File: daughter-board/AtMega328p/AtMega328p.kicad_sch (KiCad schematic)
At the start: 49 parts, among them J1 Conn_02x10_Odd_Even, J2 Conn_02x10_Odd_Even, U1 STM32L462CETx, Y1 Crystal_Small

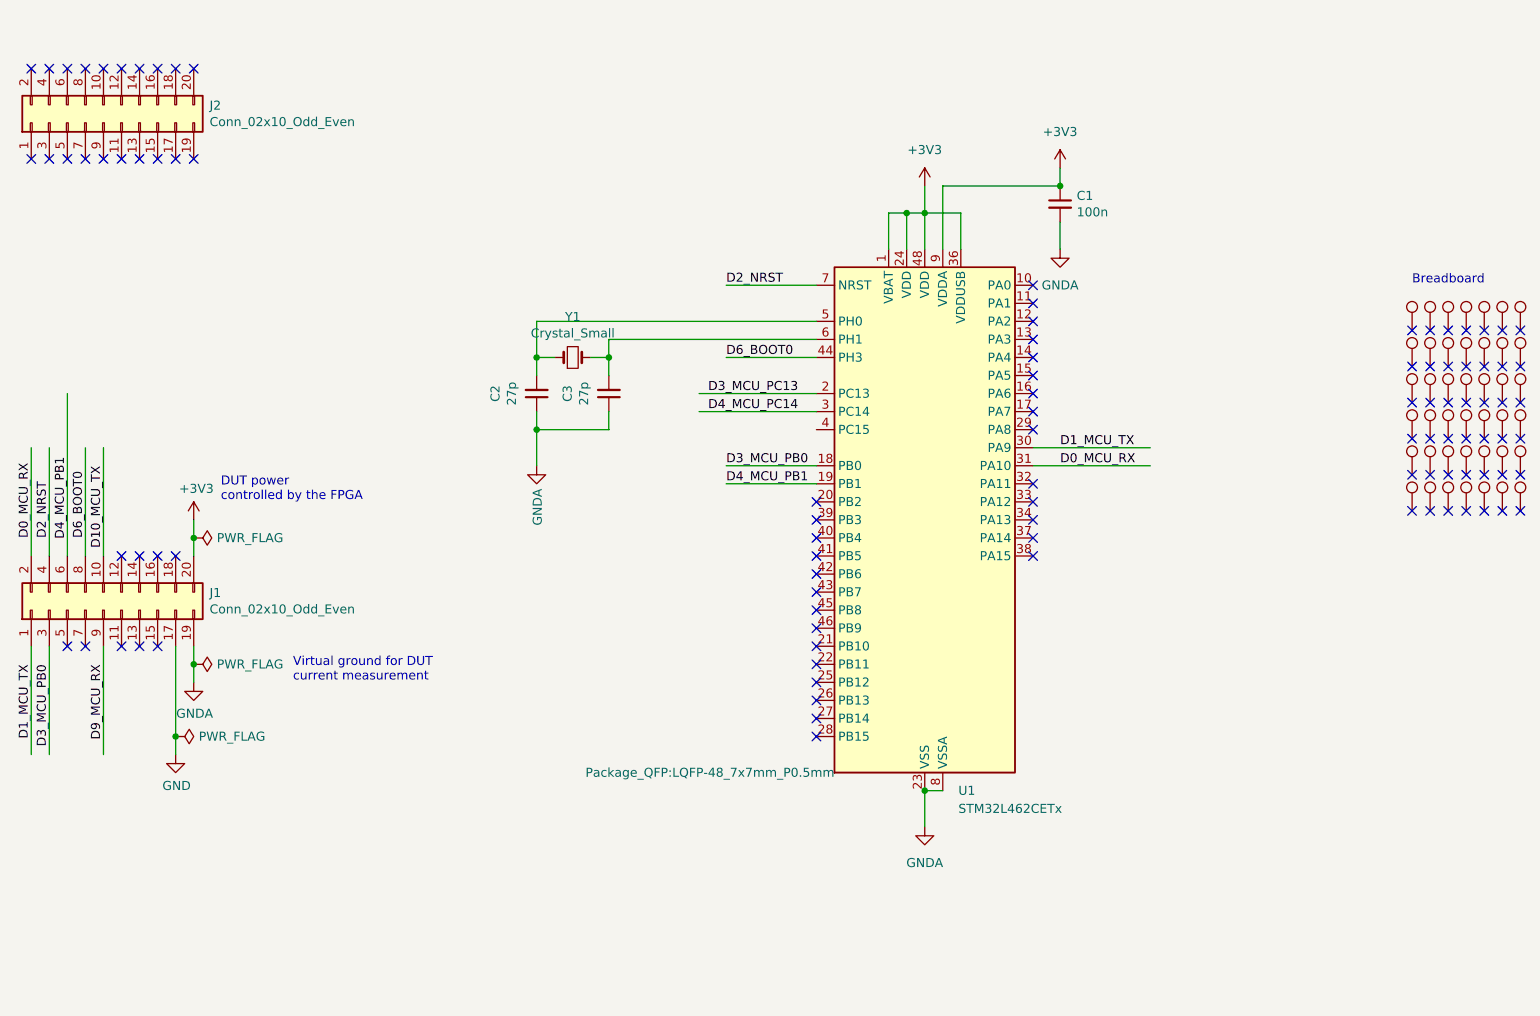
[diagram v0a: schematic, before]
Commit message: l462 routing -  Add ATMega board - Update ceval script
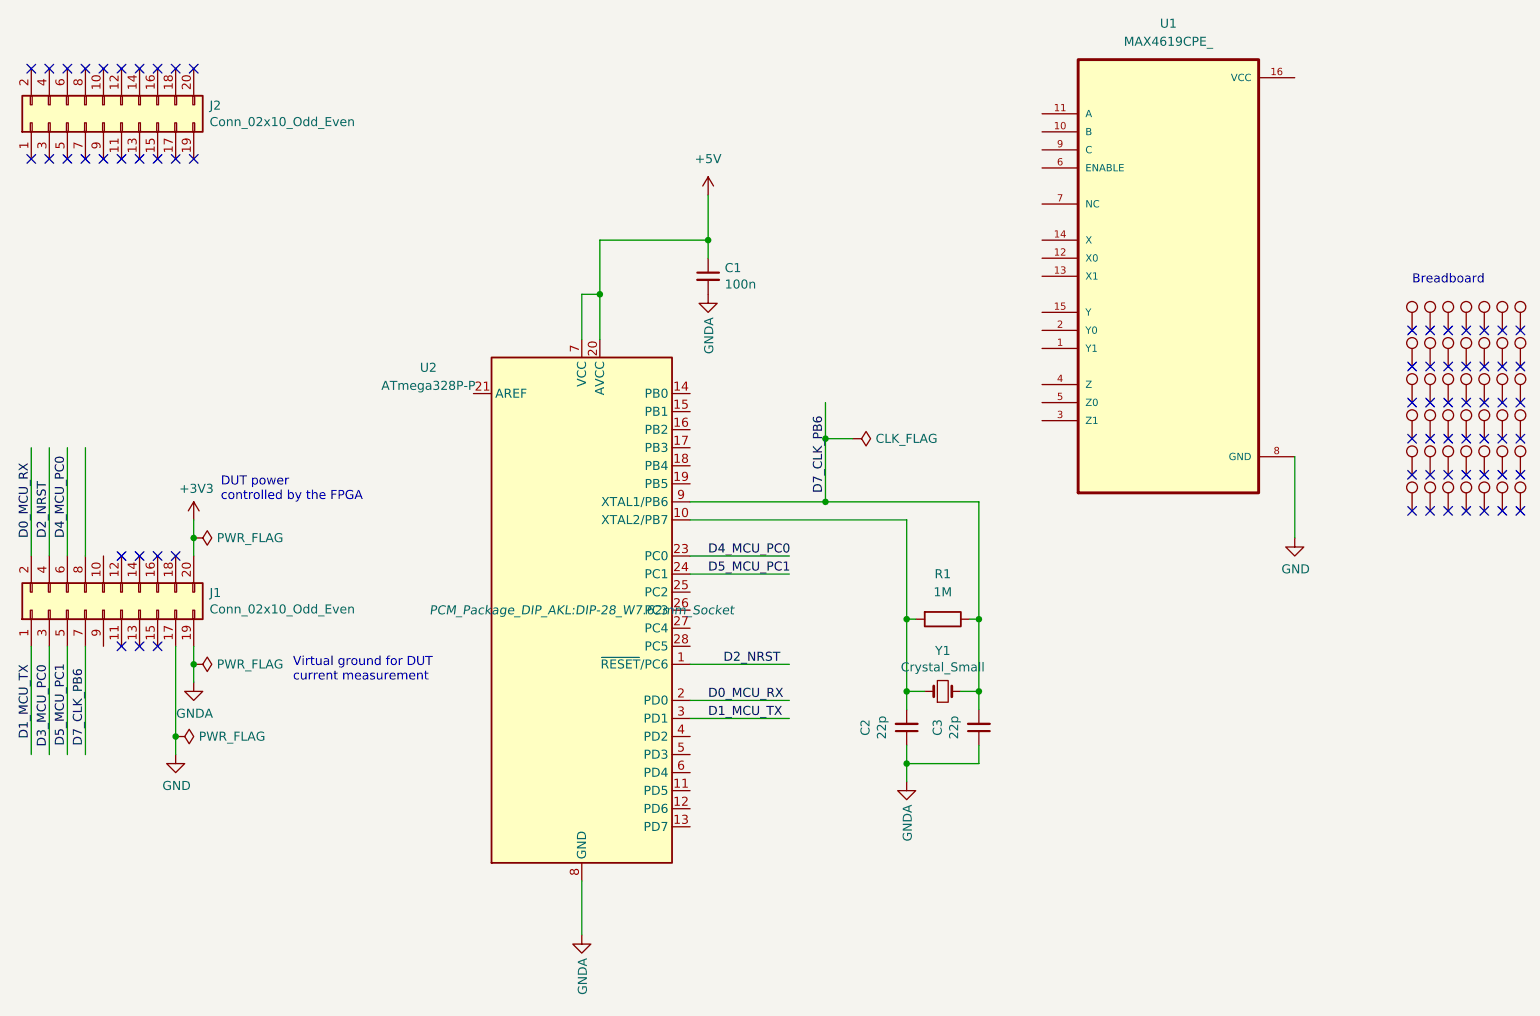
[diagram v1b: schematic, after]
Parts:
- removed U1: STM32L462CETx, Package_QFP:LQFP-48_7x7mm_P0.5mm, symbol PCM_MCU_ST_STM32L4:STM32L462CETx
- added R1: 1M, PCM_Resistor_SMD_AKL:R_0402_1005Metric, symbol Device:R
- added U1: MAX4619CPE_, MAX4619CPE_:DIP794W47P254L1943H457Q16, symbol MAX4619CPE_:MAX4619CPE_
- added U2: ATmega328P-P, PCM_Package_DIP_AKL:DIP-28_W7.62mm_Socket, symbol MCU_Microchip_ATmega:ATmega328P-P
- C1: footprint PCM_Capacitor_SMD_AKL:C_0805_2012Metric -> PCM_Capacitor_SMD_AKL:C_0201_0603Metric
- C2, C3: value 27p -> 22p
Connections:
- net +3V3: no longer C1.1
- net D0_MCU_RX: now also U2.2 (PD0)
- net D1_MCU_TX: now also U2.3 (PD1)
- net D2_NRST: now also U2.1 (~{RESET}/PC6)
- net GND: now also U1.8 (GND)
- net GNDA: now also U2.22 (GND), U2.8 (GND)
- net at C2.2, Y1.1: now also R1.2, U2.10 (XTAL2/PB7)
- net D7_CLK_PB6: now reaches C3.2, Y1.2
- net D7_CLK_PB6: now also J1.7 (Pin_7), R1.1, U2.9 (XTAL1/PB6)
- net D5_MCU_PC1: now reaches J1.5 (Pin_5)
- net D5_MCU_PC1: now also U2.24 (PC1)
- net D10_MCU_TX: no longer names the net of J1.10 (Pin_10)
- net D3_MCU_PB0 renamed D3_MCU_PC0
- net D4_MCU_PB1 renamed D4_MCU_PC0
- net D4_MCU_PC0: now also U2.23 (PC0)
- net D6_BOOT0: no longer names the net of J1.8 (Pin_8)
- net D9_MCU_RX: no longer names the net of J1.9 (Pin_9)
- new net +5V: C1.1, U2.20 (AVCC), U2.7 (VCC)
- no-connect marks 99 -> 69
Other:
- title: Scaffold STM32L462aughterboard -> Scaffold AtMega328p daughterboard
- moved on the sheet: C2, C3, Y1

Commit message: Update atmega board
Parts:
- added J3: Conn_01x03_Pin, symbol Connector:Conn_01x03_Pin
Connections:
- net +3V3 renamed VDDA
- net VDDA: now also J3.3 (Pin_3)
- net +5V: no longer names the net of C1.1, U2.20 (AVCC), U2.7 (VCC)
- net +5V: now also J3.2 (Pin_2)
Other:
- note added: "Crystal oscillator Optional if external clock present"
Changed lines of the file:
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@@
 	(wire
 		(pts
+			(xy 142.24 43.18) (xy 142.24 46.99)
+		)
+		(stroke
+			(width 0)
+			(type default)
+		)
+	)
+	(wire
+		(pts
 			(xy 172.72 111.76) (xy 173.99 111.76)
 		)
@@
 	(wire
 		(pts
+			(xy 132.08 46.99) (xy 132.08 43.18)
+		)
+		(stroke
+			(width 0)
+			(type default)
+		)
+	)
+	(wire
+		(pts
 			(xy 142.24 95.25) (xy 161.29 95.25)
 		)
@@
 	(wire
 		(pts
-			(xy 144.78 52.07) (xy 144.78 58.42)
+			(xy 144.78 43.18) (xy 144.78 58.42)
 		)
 		(stroke
@@
 	(wire
 		(pts
-			(xy 72.39 97.79) (xy 72.39 100.33)
+			(xy 72.39 93.98) (xy 72.39 100.33)
 		)
 		(stroke
@@
 	(wire
 		(pts
+			(xy 142.24 46.99) (xy 132.08 46.99)
+		)
+		(stroke
+			(width 0)
+			(type default)
+		)
+	)
+	(wire
+		(pts
 			(xy 72.39 115.57) (xy 72.39 118.11)
 		)
@@
 		)
 	)
+	(rectangle
+		(start 165.1 109.22)
+		(end 189.23 134.62)
+		(stroke
+			(width 0)
+			(type default)
+		)
+		(fill
+			(type none)
+		)
+	)
+	(rectangle
+		(start 139.7 57.15)
+		(end 152.4 66.04)
+		(stroke
+			(width 0)
+			(type default)
+		)
+		(fill
+			(type none)
+		)
+	)
 	(text "DUT power\ncontrolled by the FPGA"
 		(exclude_from_sim no)
@@
 		)
 	)
+	(text "Crystal oscillator\nOptional if external clock present "
+		(exclude_from_sim no)
+		(at 175.006 140.208 0)
+		(effects
+			(font
+				(size 1.27 1.27)
+			)
+			(justify left bottom)
+		)
+	)
 	(text "Virtual ground for DUT\ncurrent measurement"
 		(exclude_from_sim no)
@@
 				)
 				(justify right)
+				(hide yes)
 			)
 		)
@@
 				)
 				(justify right)
+				(hide yes)
 			)
 		)
@@
 	)
 	(symbol
-		(lib_id "stm32f205-rescue:+3V3-power")
-		(at 72.39 97.79 0)
-		(unit 1)
-		(exclude_from_sim no)
-		(in_bom yes)
-		(on_board yes)
-		(dnp no)
-		(property "Reference" "#PWR0101"
-			(at 72.39 101.6 0)
-			(effects
-				(font
-					(size 1.27 1.27)
-				)
-				(hide yes)
-			)
-		)
-		(property "Value" "+3V3"
-			(at 72.771 93.3958 0)
-			(effects
-				(font
-					(size 1.27 1.27)
-				)
-			)
-		)
-		(property "Footprint" ""
-			(at 72.39 97.79 0)
-			(effects
-				(font
-					(size 1.27 1.27)
-				)
-				(hide yes)
-			)
-		)
-		(property "Datasheet" ""
-			(at 72.39 97.79 0)
-			(effects
-				(font
-					(size 1.27 1.27)
-				)
-				(hide yes)
-			)
-		)
-		(property "Description" ""
-			(at 72.39 97.79 0)
-			(effects
-				(font
-					(size 1.27 1.27)
-				)
-				(hide yes)
-			)
-		)
-		(pin "1"
-		)
-		(instances
-			(project "AtMega328p"
-				(path "/4fc94e71-da2e-4d6c-a55a-b904c4759139"
-					(reference "#PWR0101")
-					(unit 1)
-				)
-			)
-		)
-	)
-	(symbol
 		(lib_id "stm32f205-rescue:GNDA-power")
 		(at 72.39 120.65 0)
@@
 	)
 	(symbol
-		(lib_id "power:+5V")
-		(at 144.78 52.07 0)
-		(unit 1)
-		(exclude_from_sim no)
-		(in_bom yes)
-		(on_board yes)
-		(dnp no)
-		(fields_autoplaced yes)
-		(property "Reference" "#PWR02"
-			(at 144.78 55.88 0)
-			(effects
-				(font
-					(size 1.27 1.27)
-				)
-				(hide yes)
-			)
-		)
-		(property "Value" "+5V"
-			(at 144.78 46.99 0)
-			(effects
-				(font
-					(size 1.27 1.27)
-				)
-			)
-		)
-		(property "Footprint" ""
-			(at 144.78 52.07 0)
-			(effects
-				(font
-					(size 1.27 1.27)
-				)
-				(hide yes)
-			)
-		)
-		(property "Datasheet" ""
-			(at 144.78 52.07 0)
-			(effects
-				(font
-					(size 1.27 1.27)
-				)
-				(hide yes)
-			)
-		)
-		(property "Description" "Power symbol creates a global label with name \"+5V\""
-			(at 144.78 52.07 0)
-			(effects
-				(font
-					(size 1.27 1.27)
-				)
-				(hide yes)
-			)
-		)
-		(pin "1"
-		)
-		(instances
-			(project "AtMega328p"
-				(path "/4fc94e71-da2e-4d6c-a55a-b904c4759139"
-					(reference "#PWR02")
-					(unit 1)
-				)
-			)
-		)
-	)
-	(symbol
 		(lib_id "MAX4619CPE_:MAX4619CPE_")
 		(at 209.55 63.5 0)
@@
 	)
 	(symbol
+		(lib_id "Connector:Conn_01x03_Pin")
+		(at 144.78 38.1 270)
+		(unit 1)
+		(exclude_from_sim no)
+		(in_bom yes)
+		(on_board yes)
+		(dnp no)
+		(fields_autoplaced yes)
+		(property "Reference" "J3"
+			(at 144.78 33.02 90)
+			(effects
+				(font
+					(size 1.27 1.27)
+				)
+			)
+		)
+		(property "Value" "Conn_01x03_Pin"
+			(at 144.78 35.56 90)
+			(effects
+				(font
+					(size 1.27 1.27)
+				)
+			)
+		)
+		(property "Footprint" ""
+			(at 144.78 38.1 0)
+			(effects
+				(font
+					(size 1.27 1.27)
+				)
+				(hide yes)
+			)
+		)
+		(property "Datasheet" "~"
+			(at 144.78 38.1 0)
+			(effects
+				(font
+					(size 1.27 1.27)
+				)
+				(hide yes)
+			)
+		)
+		(property "Description" "Generic connector, single row, 01x03, script generated"
+			(at 144.78 38.1 0)
+			(effects
+				(font
+					(size 1.27 1.27)
+				)
+				(hide yes)
+			)
+		)
+		(pin "3"
+		)
+		(pin "2"
+		)
+		(pin "1"
+		)
+		(instances
+			(project "AtMega328p"
+				(path "/4fc94e71-da2e-4d6c-a55a-b904c4759139"
+					(reference "J3")
+					(unit 1)
+				)
+			)
+		)
+	)
+	(symbol
 		(lib_id "MCU_Microchip_ATmega:ATmega328P-P")
 		(at 127 110.49 0)
@@
 		(on_board yes)
 		(dnp no)
-		(fields_autoplaced yes)
 		(property "Reference" "U2"
-			(at 105.41 76.362 0)
+			(at 113.03 73.66 0)
 			(effects
 				(font
@@
 		)
 		(property "Value" "ATmega328P-P"
-			(at 105.41 78.902 0)
+			(at 112.522 70.104 0)
 			(effects
 				(font
@@
 					(italic yes)
 				)
+				(hide yes)
 			)
 		)
@@
 	)
 	(symbol
+		(lib_id "power:VDDA")
+		(at 72.39 93.98 0)
+		(unit 1)
+		(exclude_from_sim no)
+		(in_bom yes)
+		(on_board yes)
+		(dnp no)
+		(fields_autoplaced yes)
+		(property "Reference" "#PWR03"
+			(at 72.39 97.79 0)
+			(effects
+				(font
+					(size 1.27 1.27)
+				)
+				(hide yes)
+			)
+		)
+		(property "Value" "VDDA"
+			(at 72.39 88.9 0)
+			(effects
+				(font
+					(size 1.27 1.27)
+				)
+			)
+		)
+		(property "Footprint" ""
+			(at 72.39 93.98 0)
+			(effects
+				(font
+					(size 1.27 1.27)
+				)
+				(hide yes)
+			)
+		)
+		(property "Datasheet" ""
+			(at 72.39 93.98 0)
+			(effects
+				(font
+					(size 1.27 1.27)
+				)
+				(hide yes)
+			)
+		)
+		(property "Description" "Power symbol creates a global label with name \"VDDA\""
+			(at 72.39 93.98 0)
+			(effects
+				(font
+					(size 1.27 1.27)
+				)
+				(hide yes)
+			)
+		)
+		(pin "1"
+		)
+		(instances
+			(project "AtMega328p"
+				(path "/4fc94e71-da2e-4d6c-a55a-b904c4759139"
+					(reference "#PWR03")
+					(unit 1)
+				)
+			)
+		)
+	)
+	(symbol
 		(lib_id "stm32f205-rescue:PWR_FLAG-power")
 		(at 165.1 86.36 270)
@@
 					(unit 1)
 				)
+			)
+		)
+	)
+	(symbol
+		(lib_id "power:VDDA")
+		(at 132.08 43.18 0)
+		(unit 1)
+		(exclude_from_sim no)
+		(in_bom yes)
+		(on_board yes)
+		(dnp no)
+		(fields_autoplaced yes)
+		(property "Reference" "#PWR02"
+			(at 132.08 46.99 0)
+			(effects
+				(font
+					(size 1.27 1.27)
+				)
+				(hide yes)
+			)
+		)
+		(property "Value" "VDDA"
+			(at 132.08 38.1 0)
+			(effects
+				(font
+					(size 1.27 1.27)
+				)
+			)
+		)
+		(property "Footprint" ""
+			(at 132.08 43.18 0)
+			(effects
+				(font
+					(size 1.27 1.27)
+				)
+				(hide yes)
+			)
+		)
+		(property "Datasheet" ""
+			(at 132.08 43.18 0)
+			(effects
+				(font
+					(size 1.27 1.27)
+				)
+				(hide yes)
+			)
+		)
+		(property "Description" "Power symbol creates a global label with name \"VDDA\""
+			(at 132.08 43.18 0)
+			(effects
+				(font
+					(size 1.27 1.27)
+				)
+				(hide yes)
+			)
+		)
+		(pin "1"
+		)
+		(instances
+			(project "AtMega328p"
+				(path "/4fc94e71-da2e-4d6c-a55a-b904c4759139"
+					(reference "#PWR02")
+					(unit 1)
+				)
